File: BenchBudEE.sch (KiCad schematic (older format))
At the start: 0 parts

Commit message: LED Driver Module
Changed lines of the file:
@@
 F0 "LED_Driver" 50
 F1 "LED_Driver.sch" 50
-F2 "EN" I L 6950 2800 60
-F3 "FREQ" I L 6950 3050 60
-F4 "String+" O R 8850 2800 60
-F5 "String-" I R 8850 3150 60
+F2 "String+" O R 8850 2800 60
+F3 "String-" I R 8850 3150 60
+F4 "LED_EN_PWM" I L 6950 2800 60
 $EndSheet
 $Sheet

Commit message: Arduino Modules
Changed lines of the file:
@@
 Sheet 1 9
 Title ""
-Date "22 may 2014"
+Date "24 may 2014"
 Rev ""
 Comp ""
@@
 F0 "Arduino" 50
 F1 "Arduino.sch" 50
-F2 "Relay+" O R 3450 6900 60
+F2 "Relay+" O R 3450 6400 60
 F3 "Relay-" I R 3450 6700 60
-F4 "SCLK" O R 3450 6350 60
-F5 "CS_N" O R 3450 6200 60
-F6 "MOSI" O R 3450 6050 60
-F7 "MISO" I R 3450 5900 60
-F8 "LED_EN" O R 3450 5500 60
-F9 "LED_FREQ" O R 3450 5300 60
-F10 "FAN_EN" O R 3450 4750 60
-F11 "TACH_MEAS" I R 3450 4600 60
-$EndSheet
-$Sheet
-S 6950 4100 1950 1350
+F4 "SCLK" O R 3450 4700 60
+F5 "MOSI" O R 3450 4300 60
+F6 "MISO" I R 3450 4400 60
+F7 "TACH_MEAS" I R 3450 5200 60
+F8 "FAN_EN_N" O R 3450 4100 60
+F9 "CURR_MEAS" I R 3450 5400 60
+F10 "V+_ADJ_MON" I R 3450 3750 60
+F11 "V-_ADJ_MON" I R 3450 3900 60
+F12 "LED_EN_PWM" O R 3450 5900 60
+F13 "DAC_CS_N" O R 3450 4500 60
+F14 "ADC_CS_N" O R 3450 4900 60
+$EndSheet
+$Sheet
+S 7150 3000 1500 1000
 U 537AC610
 F0 "Thermocouple" 50
 F1 "Thermocouple.sch" 50
-F2 "TC IN-" I R 8900 4550 60
-F3 "TC IN+" I R 8900 4400 60
-F4 "MOSI" I L 6950 4400 60
-F5 "MISO" O L 6950 4550 60
-F6 "SCLK" I L 6950 4750 60
-F7 "CS_N" I L 6950 4900 60
+F2 "TC IN-" I R 8650 3500 60
+F3 "TC IN+" I R 8650 3300 60
+F4 "MOSI" I L 7150 3300 60
+F5 "MISO" O L 7150 3450 60
+F6 "SCLK" I L 7150 3650 60
+F7 "CS_N" I L 7150 3800 60
 $EndSheet
 $Sheet
@@
 $EndSheet
 $Sheet
-S 6950 2450 1900 1400
+S 7100 4400 1850 900
 U 537AC6DF
 F0 "LED_Driver" 50
 F1 "LED_Driver.sch" 50
-F2 "String+" O R 8850 2800 60
-F3 "String-" I R 8850 3150 60
-F4 "LED_EN_PWM" I L 6950 2800 60
-$EndSheet
-$Sheet
-S 7100 700  1500 1600
+F2 "LED_EN_PWM" I L 7100 4900 60
+F3 "LED_STRING+" O R 8950 4600 60
+F4 "LED_STRING-" O R 8950 4700 60
+$EndSheet
+$Sheet
+S 7150 1100 1500 1600
 U 537AC712
 F0 "Fan" 50
 F1 "Fan.sch" 50
-F2 "Power+" O R 8600 1150 60
-F3 "Power-" I R 8600 1400 60
-F4 "Tach" I R 8600 1700 60
-F5 "Tach_out" O L 7100 2200 60
-F6 "Fan_In" I L 7100 1050 60
-F7 "Current_Measure" O L 7100 2000 60
-F8 "MOSI" I L 7100 1200 60
-F9 "MISO" O L 7100 1400 60
-F10 "CS_N" I L 7100 1600 60
-F11 "SCLK" I L 7100 1800 60
-$EndSheet
-$Sheet
-S 9550 1350 850  4600
+F2 "MOSI" I L 7150 1600 60
+F3 "MISO" O L 7150 1800 60
+F4 "CS_N" I L 7150 2000 60
+F5 "SCLK" I L 7150 2200 60
+F6 "FAN_OUT+" O R 8650 1200 60
+F7 "TACH_MEAS" O L 7150 2450 60
+F8 "CURR_MEAS" O L 7150 2600 60
+F9 "TACH_IN" I R 8650 1700 60
+F10 "FAN_EN_N" I L 7150 1300 60
+F11 "FAN_OUT-" O R 8650 1300 60
+$EndSheet
+$Sheet
+S 9550 550  750  6400
 U 537AD028
 F0 "TerminalBlock" 50
 F1 "TerminalBlock.sch" 50
-$EndSheet
-$Sheet
-S 7100 5650 1600 1000
+F2 "V+_ADJ" I L 9550 700 60
+F3 "V-_ADJ" I L 9550 800 60
+F4 "FAN_OUT+" O L 9550 1200 60
+F5 "FAN_OUT-" I L 9550 1300 60
+F6 "TACH_IN" I L 9550 1700 60
+F7 "LED_STRING+" O L 9550 4600 60
+F8 "LED_STRING-" O L 9550 4700 60
+F9 "TC_IN+" I L 9550 3300 60
+F10 "TC_IN-" I L 9550 3500 60
+F11 "RELAY_COM" B L 9550 6100 60
+F12 "RELAY_NC" B L 9550 5750 60
+F13 "RELAY_NO" B L 9550 5900 60
+$EndSheet
+$Sheet
+S 7100 5550 1600 1000
 U 537AD218
 F0 "Relay" 50
 F1 "Relay.sch" 50
-F2 "DIN+" I L 7100 5900 60
-F3 "DIN-" O L 7100 6150 60
-F4 "Relay+" I R 8700 5900 60
-F5 "Relay-" O R 8700 6150 60
-$EndSheet
-$Sheet
-S 3900 900  1950 1500
+F2 "RELAY_NC" B R 8700 5750 60
+F3 "RELAY_NO" B R 8700 5900 60
+F4 "RELAY_COM" B R 8700 6100 60
+F5 "Relay+" I L 7100 5800 60
+F6 "Relay-" O L 7100 6050 60
+$EndSheet
+$Sheet
+S 4200 600  1650 1650
 U 537D725F
 F0 "PowerAdjustmentMonitor" 50
 F1 "PowerAdjustmentMonitor.sch" 50
-F2 "V+_ADJ" O R 5850 1350 60
-F3 "V-_ADJ" O R 5850 1500 60
-F4 "3V3_MON" O R 5850 1700 60
-F5 "5V_MON" O R 5850 1900 60
-F6 "V+_ADJ_MON" O R 5850 2000 60
-F7 "V-_ADJ_MON" O R 5850 2100 60
-F8 "V+_CURR_MON" O R 5850 2200 60
-F9 "V-_CURR_MON" O R 5850 2300 60
-$EndSheet
+F2 "V+_ADJ" O R 5850 700 60
+F3 "V-_ADJ" O R 5850 800 60
+F4 "3V3_MON" O L 4200 1100 60
+F5 "5V_MON" O L 4200 1300 60
+F6 "V+_ADJ_MON" O L 4200 1600 60
+F7 "V-_ADJ_MON" O L 4200 1750 60
+F8 "V+_CURR_MON" O L 4200 1900 60
+F9 "V-_CURR_MON" O L 4200 2050 60
+$EndSheet
+Wire Wire Line
+	5850 700  9550 700
+Wire Wire Line
+	5850 800  9550 800
+Wire Wire Line
+	8650 1200 9550 1200
+Wire Wire Line
+	8650 1300 9550 1300
+Wire Wire Line
+	9550 1300 9550 1250
+Wire Wire Line
+	8650 1700 9550 1700
+Wire Wire Line
+	8700 5750 9550 5750
+Wire Wire Line
+	8700 5900 9550 5900
+Wire Wire Line
+	8700 6100 9550 6100
+Wire Wire Line
+	3450 3750 3900 3750
+Wire Wire Line
+	3900 3750 3900 1600
+Wire Wire Line
+	3900 1600 4200 1600
+Wire Wire Line
+	3450 3900 4000 3900
+Wire Wire Line
+	4000 3900 4000 1750
+Wire Wire Line
+	4000 1750 4200 1750
+Wire Wire Line
+	3450 4100 6800 4100
+Wire Wire Line
+	6800 4100 6800 1300
+Wire Wire Line
+	6800 1300 7150 1300
+Wire Wire Line
+	3450 4700 6600 4700
+Wire Wire Line
+	6600 4700 6600 2200
+Wire Wire Line
+	6600 2200 7150 2200
+Wire Wire Line
+	3450 5200 6150 5200
+Wire Wire Line
+	6150 5200 6150 2450
+Wire Wire Line
+	6150 2450 7150 2450
+Wire Wire Line
+	3450 5400 6900 5400
+Wire Wire Line
+	6900 5400 6900 2600
+Wire Wire Line
+	6900 2600 7150 2600
+Wire Wire Line
+	8650 3300 9550 3300
+Wire Wire Line
+	8650 3500 9550 3500
+Wire Wire Line
+	8950 4600 9550 4600
+Wire Wire Line
+	8950 4700 9550 4700
+Wire Wire Line
+	3450 4300 6300 4300
+Wire Wire Line
+	6300 4300 6300 1600
+Wire Wire Line
+	6300 1600 7150 1600
+Wire Wire Line
+	3450 4400 6400 4400
+Wire Wire Line
+	6400 4400 6400 1800
+Wire Wire Line
+	6400 1800 7150 1800
+Wire Wire Line
+	7150 3300 6300 3300
+Connection ~ 6300 3300
+Wire Wire Line
+	7150 3450 6400 3450
+Connection ~ 6400 3450
+Wire Wire Line
+	7150 3650 6600 3650
+Connection ~ 6600 3650
+Wire Wire Line
+	3450 5900 6800 5900
+Wire Wire Line
+	6800 5900 6800 4900
+Wire Wire Line
+	6800 4900 7100 4900
+Wire Wire Line
+	3450 4500 6500 4500
+Wire Wire Line
+	6500 4500 6500 2000
+Wire Wire Line
+	6500 2000 7150 2000
+Wire Wire Line
+	3450 4900 6700 4900
+Wire Wire Line
+	6700 4900 6700 3800
+Wire Wire Line
+	6700 3800 7150 3800
+Wire Wire Line
+	3450 6400 6900 6400
+Wire Wire Line
+	6900 6400 6900 5800
+Wire Wire Line
+	6900 5800 7100 5800
+Wire Wire Line
+	3450 6700 7000 6700
+Wire Wire Line
+	7000 6700 7000 6050
+Wire Wire Line
+	7000 6050 7100 6050
 $EndSCHEMATC

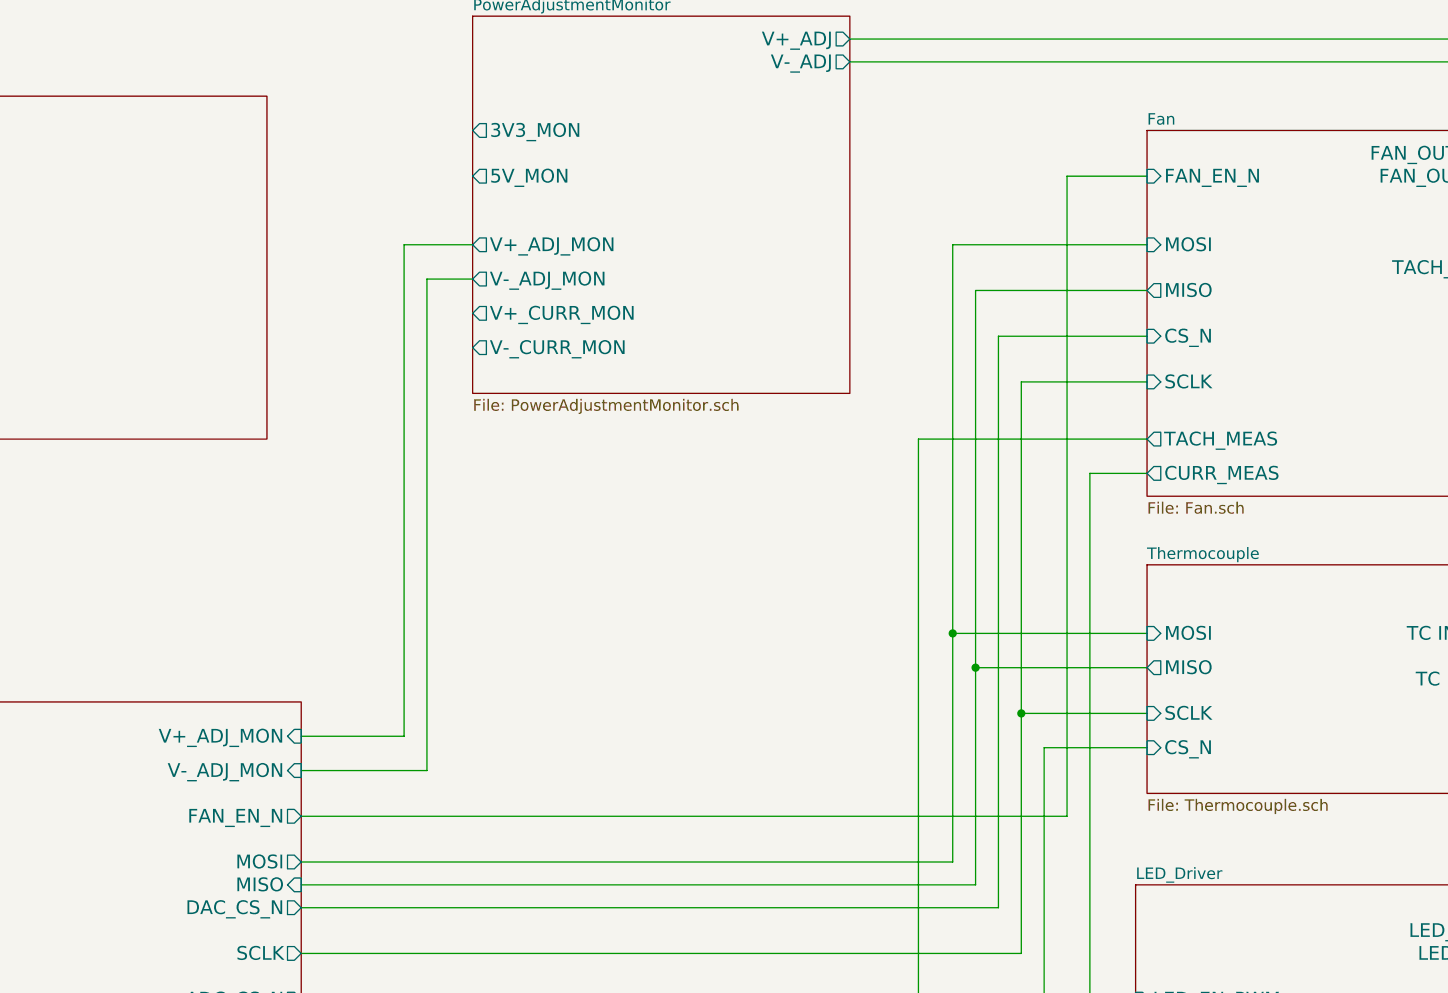
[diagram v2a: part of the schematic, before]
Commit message: Fan/Current Module Refactoring
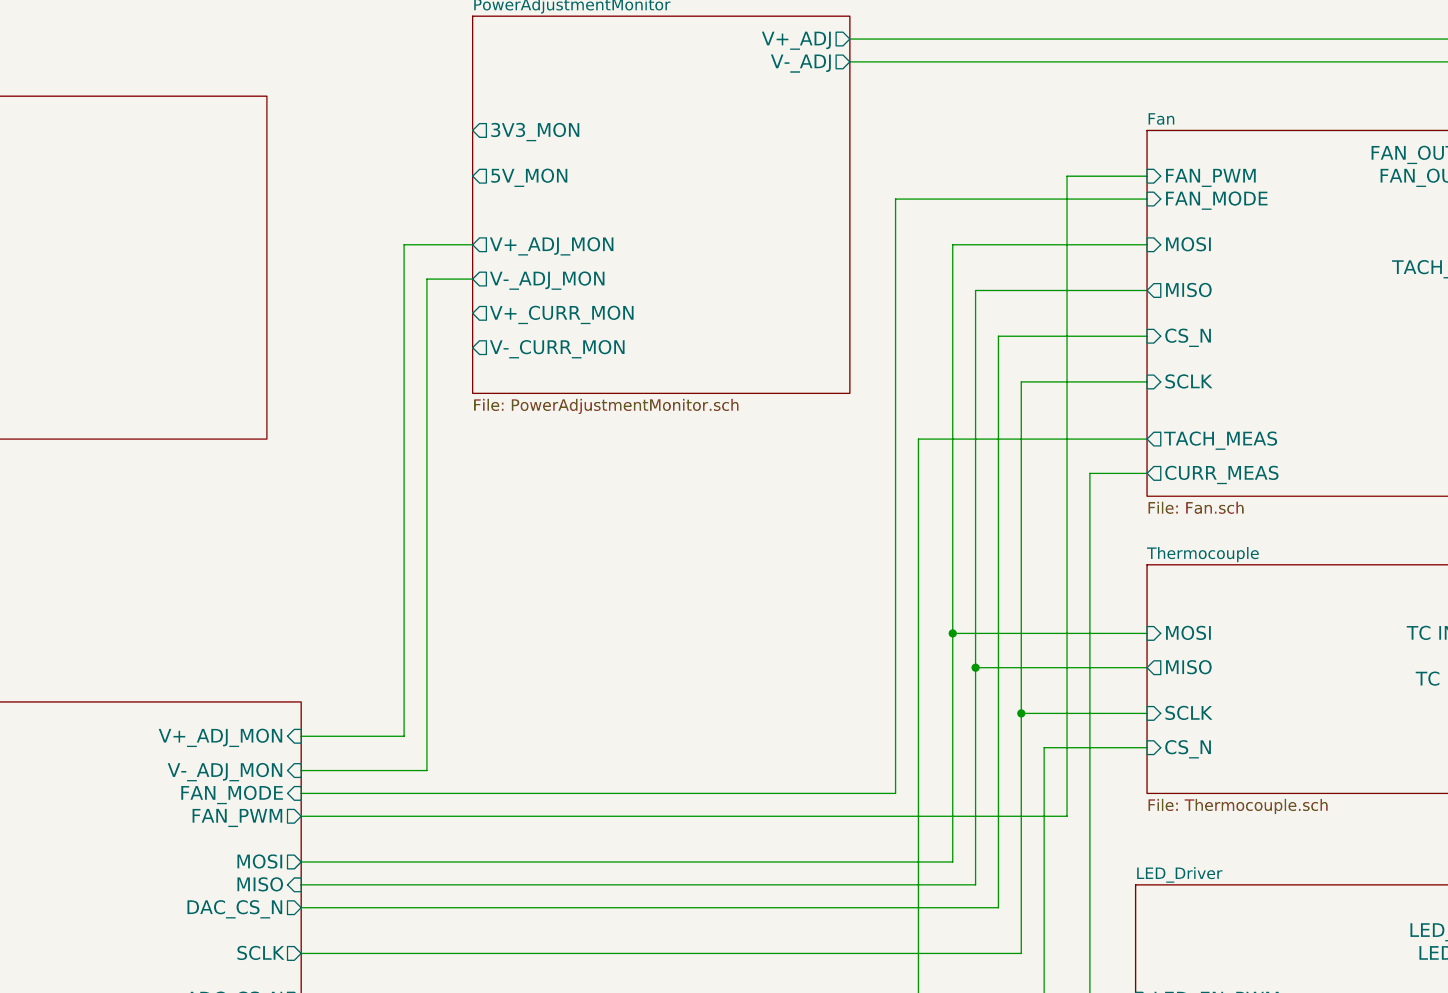
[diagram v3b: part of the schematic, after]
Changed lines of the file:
@@
 Sheet 1 9
 Title ""
-Date "24 may 2014"
+Date "25 may 2014"
 Rev ""
 Comp ""
@@
 F6 "MISO" I R 3450 4400 60
 F7 "TACH_MEAS" I R 3450 5200 60
-F8 "FAN_EN_N" O R 3450 4100 60
-F9 "CURR_MEAS" I R 3450 5400 60
-F10 "V+_ADJ_MON" I R 3450 3750 60
-F11 "V-_ADJ_MON" I R 3450 3900 60
-F12 "LED_EN_PWM" O R 3450 5900 60
-F13 "DAC_CS_N" O R 3450 4500 60
-F14 "ADC_CS_N" O R 3450 4900 60
+F8 "CURR_MEAS" I R 3450 5400 60
+F9 "V+_ADJ_MON" I R 3450 3750 60
+F10 "V-_ADJ_MON" I R 3450 3900 60
+F11 "LED_EN_PWM" O R 3450 5900 60
+F12 "DAC_CS_N" O R 3450 4500 60
+F13 "ADC_CS_N" O R 3450 4900 60
+F14 "FAN_PWM" O R 3450 4100 60
+F15 "FAN_MODE" I R 3450 4000 60
 $EndSheet
 $Sheet
@@
 F8 "CURR_MEAS" O L 7150 2600 60
 F9 "TACH_IN" I R 8650 1700 60
-F10 "FAN_EN_N" I L 7150 1300 60
-F11 "FAN_OUT-" O R 8650 1300 60
+F10 "FAN_OUT-" O R 8650 1300 60
+F11 "FAN_PWM" I L 7150 1300 60
+F12 "FAN_MODE" I L 7150 1400 60
 $EndSheet
 $Sheet
@@
 Wire Wire Line
 	7000 6050 7100 6050
+Wire Wire Line
+	3450 4000 6050 4000
+Wire Wire Line
+	6050 4000 6050 1400
+Wire Wire Line
+	6050 1400 7150 1400
 $EndSCHEMATC
